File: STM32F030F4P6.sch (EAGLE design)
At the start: 11 parts, among them J3 455-1750-1-ND, U1 STM32F030F4P6, U2 CJA1117B-3.3-SOT89

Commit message: Initial commit.
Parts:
- J1: device SparkFun-Connectors:CONN_10" -> SparkFun-Connectors:CONN_11
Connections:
- new net N$1: J2.7
- new net N$2: J2.8
- new net VIN_5-30V: J1.1
- net A0: now also J1.7; no longer J1.6
- net A1: now also J1.8; no longer J1.7
- net A10: now also J2.6; no longer J2.3
- net A2: now also J1.9; no longer J1.8
- net A3: now also J1.10; no longer J1.9
- net A4: now also J1.11; no longer J1.10
- net A5: now also J2.1; no longer J2.10
- net A6: now also J2.2; no longer J2.9
- net A7: now also J2.3; no longer J2.8
- net A9: now also J2.5; no longer J2.4
- net B1: now also J2.4; no longer J2.7
- net BOOT0: now also J1.2; no longer J1.1
- net GND: no longer J2.6
- net NRST: now also J1.5; no longer J1.4
- net OSC_IN: now also J1.3; no longer J1.2
- net OSC_OUT: now also J1.4; no longer J1.3
- net SWCLK: now also J2.10; no longer J2.1
- net SWDIO: now also J2.9; no longer J2.2
- net VDD: no longer J2.5
- net VDDA: now also J1.6; no longer J1.5
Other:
- moved on the sheet: J2, J3

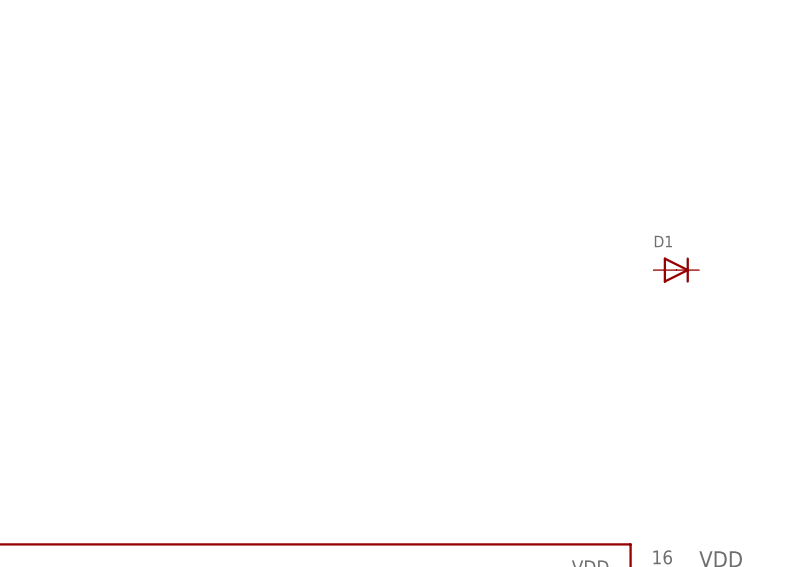
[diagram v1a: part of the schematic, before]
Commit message: Added J-Link connector.
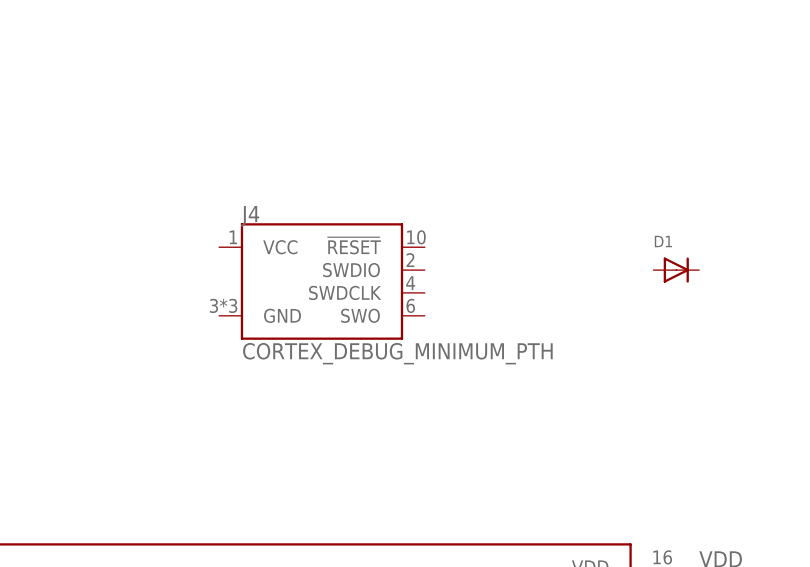
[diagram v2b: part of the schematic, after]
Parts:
- added J4: CORTEX_DEBUG_MINIMUM_PTH, SparkFun-Connectors:CORTEX_DEBUG_MINIMUM_PTH
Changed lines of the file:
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@@
 <part name="J1" library="SparkFun-Connectors" deviceset="CONN_11" device=""/>
 <part name="J2" library="SparkFun-Connectors" deviceset="CONN_10" device="&quot;"/>
+<part name="J4" library="SparkFun-Connectors" deviceset="CORTEX_DEBUG_MINIMUM" device="_PTH"/>
 </parts>
 <sheets>
@@
 <attribute name="NAME" x="91.44" y="93.472" size="1.778" layer="95" font="vector" rot="MR180"/>
 </instance>
+<instance part="J4" gate="G$1" x="147.32" y="109.22" smashed="yes">
+<attribute name="NAME" x="137.16" y="117.094" size="1.778" layer="95" font="vector"/>
+<attribute name="VALUE" x="137.16" y="101.854" size="1.778" layer="96" font="vector"/>
+</instance>
 </instances>

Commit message: Added capacitors, resistors, diodes, LEDs.
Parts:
- added C2, C3, C4, C5, C6, C7: (no value), adafruit:C-USC0603
- added D2: (no value), adafruit:DIODESOD-123
- added LED2: (no value), adafruit:LEDCHIPLED_0603
- added R2, R3, R4, R5: (no value), adafruit:R-US_R0603
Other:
- moved on the sheet: C1
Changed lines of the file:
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@@
 <part name="J2" library="SparkFun-Connectors" deviceset="CONN_10" device="&quot;"/>
 <part name="J4" library="SparkFun-Connectors" deviceset="CORTEX_DEBUG_MINIMUM" device="_PTH"/>
+<part name="R2" library="adafruit" deviceset="R-US_" device="R0603"/>
+<part name="R3" library="adafruit" deviceset="R-US_" device="R0603"/>
+<part name="R4" library="adafruit" deviceset="R-US_" device="R0603"/>
+<part name="C2" library="adafruit" deviceset="C-US" device="C0603"/>
+<part name="C3" library="adafruit" deviceset="C-US" device="C0603"/>
+<part name="C4" library="adafruit" deviceset="C-US" device="C0603"/>
+<part name="C5" library="adafruit" deviceset="C-US" device="C0603"/>
+<part name="C6" library="adafruit" deviceset="C-US" device="C0603"/>
+<part name="C7" library="adafruit" deviceset="C-US" device="C0603"/>
+<part name="LED2" library="adafruit" deviceset="LED" device="CHIPLED_0603"/>
+<part name="R5" library="adafruit" deviceset="R-US_" device="R0603"/>
+<part name="D2" library="adafruit" deviceset="DIODE" device="SOD-123"/>
 </parts>
 <sheets>
@@
 </plain>
 <instances>
-<instance part="C1" gate="G$1" x="71.12" y="15.24" smashed="yes">
-<attribute name="NAME" x="72.136" y="15.875" size="1.778" layer="95"/>
-<attribute name="VALUE" x="72.136" y="11.049" size="1.778" layer="96"/>
+<instance part="C1" gate="G$1" x="22.86" y="17.78" smashed="yes">
+<attribute name="NAME" x="23.876" y="18.415" size="1.778" layer="95"/>
+<attribute name="VALUE" x="23.876" y="13.589" size="1.778" layer="96"/>
 </instance>
 <instance part="R1" gate="G$1" x="99.06" y="15.24" smashed="yes">
@@
 <attribute name="VALUE" x="137.16" y="101.854" size="1.778" layer="96" font="vector"/>
 </instance>
+<instance part="R2" gate="G$1" x="99.06" y="10.16" smashed="yes">
+<attribute name="NAME" x="95.25" y="11.6586" size="1.778" layer="95"/>
+<attribute name="VALUE" x="95.25" y="6.858" size="1.778" layer="96"/>
+</instance>
+<instance part="R3" gate="G$1" x="99.06" y="5.08" smashed="yes">
+<attribute name="NAME" x="95.25" y="6.5786" size="1.778" layer="95"/>
+<attribute name="VALUE" x="95.25" y="1.778" size="1.778" layer="96"/>
+</instance>
+<instance part="R4" gate="G$1" x="99.06" y="0" smashed="yes">
+<attribute name="NAME" x="95.25" y="1.4986" size="1.778" layer="95"/>
+<attribute name="VALUE" x="95.25" y="-3.302" size="1.778" layer="96"/>
+</instance>
+<instance part="C2" gate="G$1" x="30.48" y="17.78" smashed="yes">
+<attribute name="NAME" x="31.496" y="18.415" size="1.778" layer="95"/>
+<attribute name="VALUE" x="31.496" y="13.589" size="1.778" layer="96"/>
+</instance>
+<instance part="C3" gate="G$1" x="38.1" y="17.78" smashed="yes">
+<attribute name="NAME" x="39.116" y="18.415" size="1.778" layer="95"/>
+<attribute name="VALUE" x="39.116" y="13.589" size="1.778" layer="96"/>
+</instance>
+<instance part="C4" gate="G$1" x="45.72" y="17.78" smashed="yes">
+<attribute name="NAME" x="46.736" y="18.415" size="1.778" layer="95"/>
+<attribute name="VALUE" x="46.736" y="13.589" size="1.778" layer="96"/>
+</instance>
+<instance part="C5" gate="G$1" x="53.34" y="17.78" smashed="yes">
+<attribute name="NAME" x="54.356" y="18.415" size="1.778" layer="95"/>
+<attribute name="VALUE" x="54.356" y="13.589" size="1.778" layer="96"/>
+</instance>
+<instance part="C6" gate="G$1" x="60.96" y="17.78" smashed="yes">
+<attribute name="NAME" x="61.976" y="18.415" size="1.778" layer="95"/>
+<attribute name="VALUE" x="61.976" y="13.589" size="1.778" layer="96"/>
+</instance>
+<instance part="C7" gate="G$1" x="68.58" y="17.78" smashed="yes">
+<attribute name="NAME" x="69.596" y="18.415" size="1.778" layer="95"/>
+<attribute name="VALUE" x="69.596" y="13.589" size="1.778" layer="96"/>
+</instance>
+<instance part="LED2" gate="G$1" x="129.54" y="17.78" smashed="yes" rot="MR0">
+<attribute name="NAME" x="125.984" y="13.208" size="1.778" layer="95" rot="MR90"/>
+<attribute name="VALUE" x="123.825" y="13.208" size="1.778" layer="96" rot="MR90"/>
+</instance>
+<instance part="R5" gate="G$1" x="99.06" y="-5.08" smashed="yes">
+<attribute name="NAME" x="95.25" y="-3.5814" size="1.778" layer="95"/>
+<attribute name="VALUE" x="95.25" y="-8.382" size="1.778" layer="96"/>
+</instance>
+<instance part="D2" gate="G$1" x="185.42" y="106.68" smashed="yes">
+<attribute name="NAME" x="182.88" y="109.22" size="1.27" layer="95"/>
+<attribute name="VALUE" x="182.88" y="102.87" size="1.27" layer="96"/>
+</instance>
 </instances>
